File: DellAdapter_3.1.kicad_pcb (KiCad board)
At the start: 2 copper layers, 63.2 x 20.8 mm, 19 parts, among them J1 USB4065-XX-X_REVA, J2 USB4151-GF-C_REVA

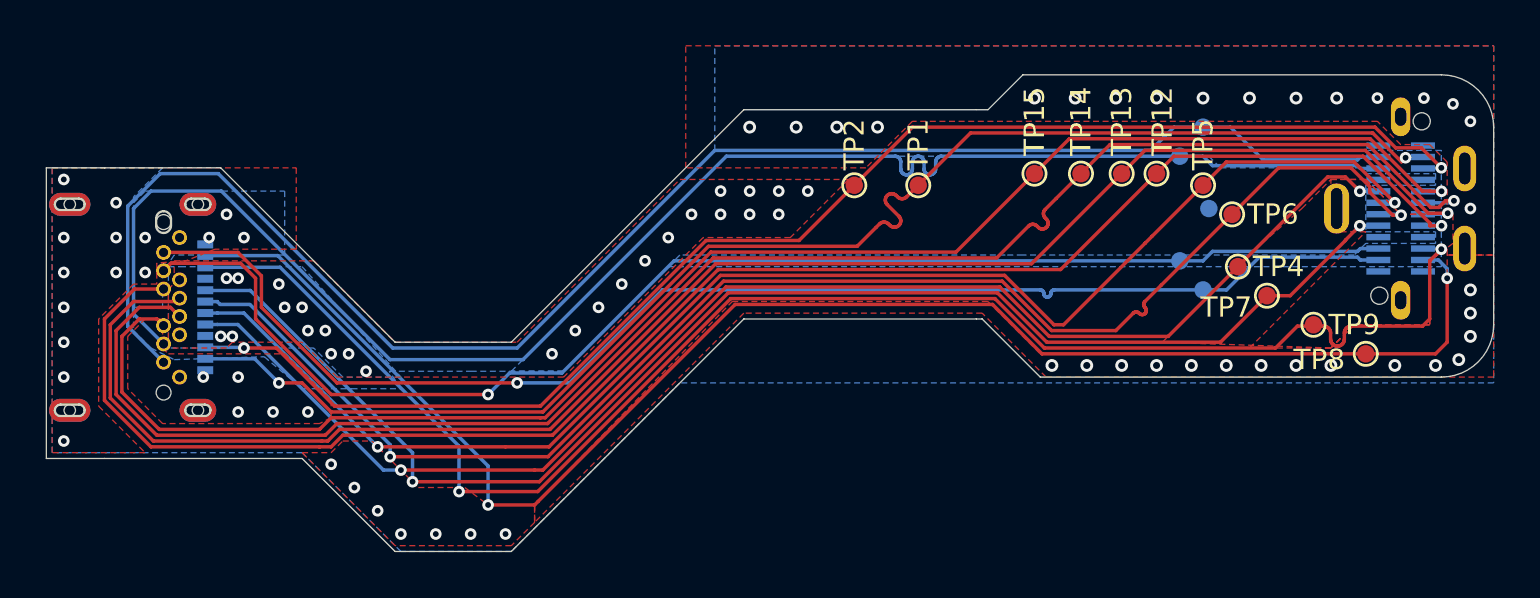
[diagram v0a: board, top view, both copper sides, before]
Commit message: increase pad size; panelize
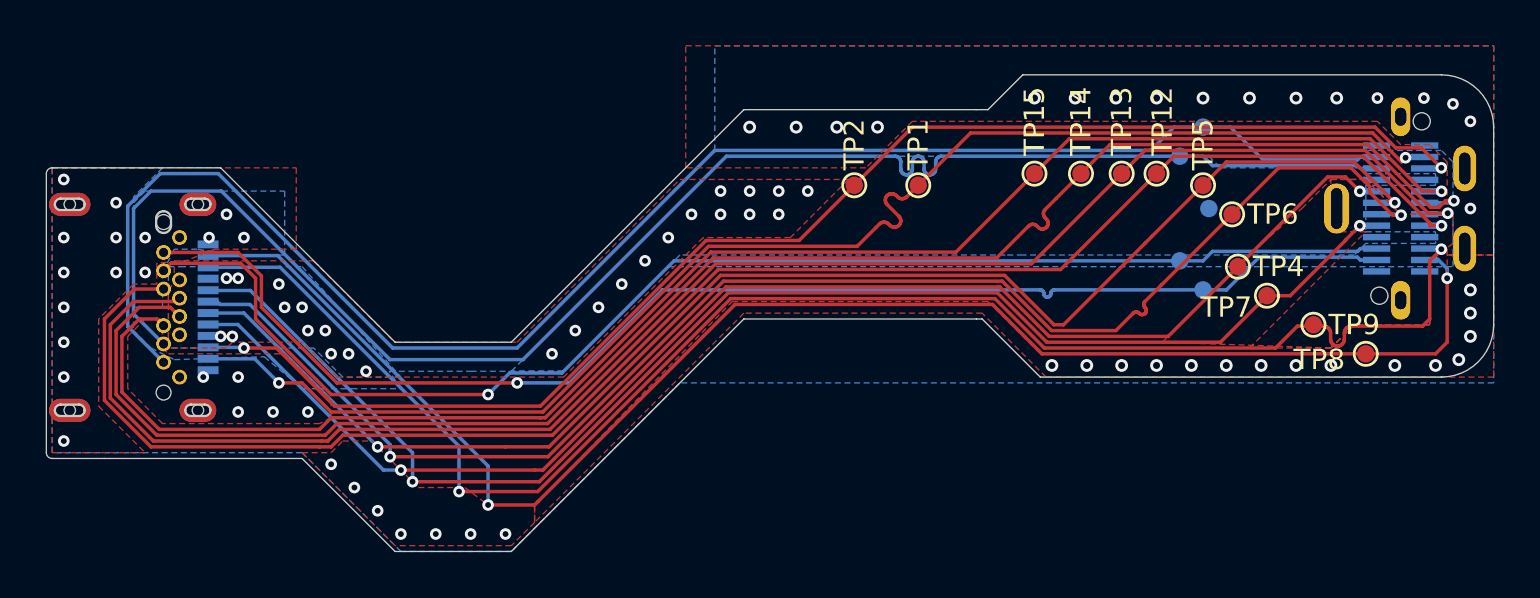
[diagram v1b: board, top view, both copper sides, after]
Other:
- outline, holes or cut-outs redrawn
- board text added: "Rev. 3.2 - 5 Dec 2020"
- board text removed: "Rev. 3.1 - 10 Nov 2020"
